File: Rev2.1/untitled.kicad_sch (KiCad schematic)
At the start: 29 parts, among them SW1 SW_Push, SW2 SW_SPDT, U5 AMS1117-3.3, Y1 16MHz

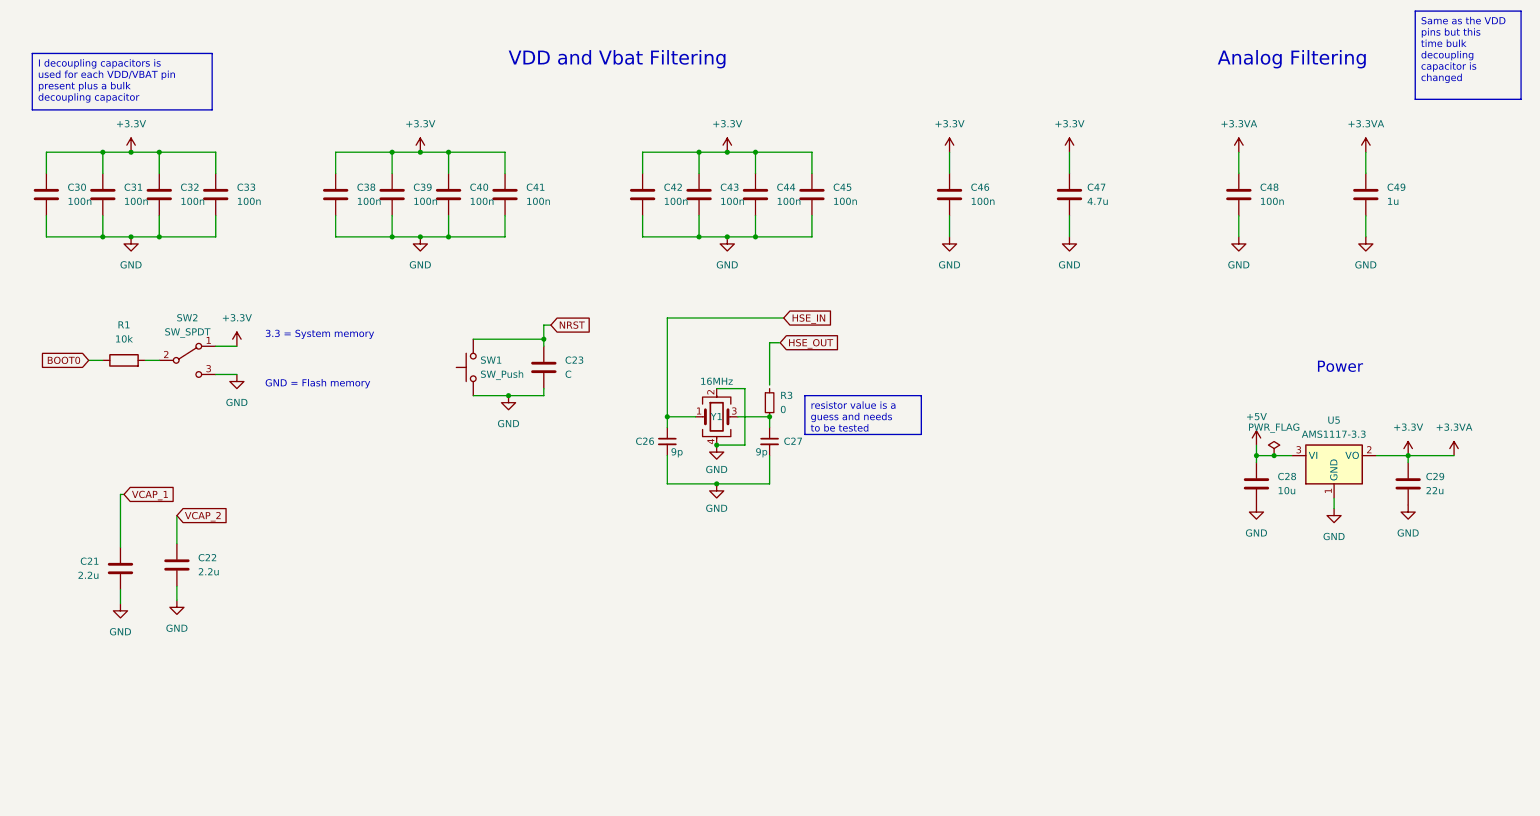
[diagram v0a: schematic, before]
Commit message: re-adding files something happened with last commit
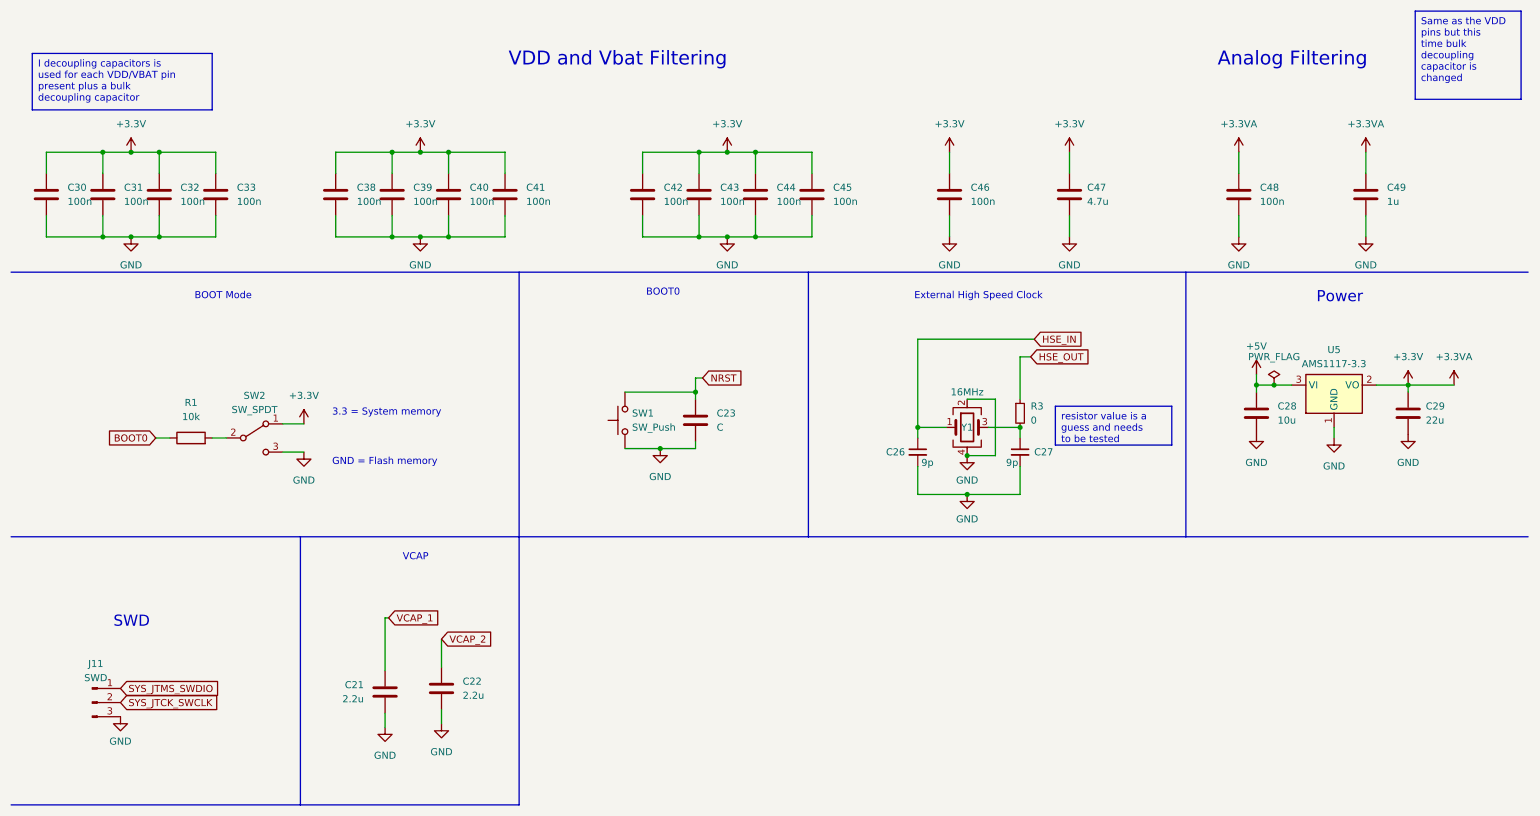
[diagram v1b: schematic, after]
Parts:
- added J11: SWD, Connector_PinHeader_2.54mm:PinHeader_1x03_P2.54mm_Vertical, symbol Connector:Conn_01x03_Pin
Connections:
- net GND: now also J11.3 (Pin_3)
- net HSE_OUT: now also R3.1
- new net SYS_JTCK_SWCLK: J11.2 (Pin_2)
- new net SYS_JTMS_SWDIO: J11.1 (Pin_1)
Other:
- note added: "BOOT Mode"
- note added: "BOOT0"
- note added: "External High Speed Clock"
- note added: "SWD"
- note added: "VCAP"
- moved on the sheet: C21, C22, C23, C26, C27, C28, C29, R1, R3, SW1, SW2, U5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

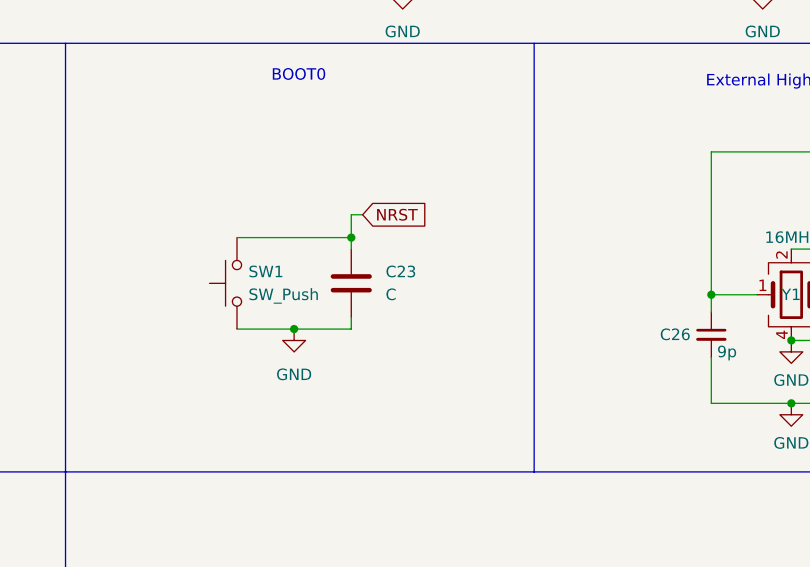
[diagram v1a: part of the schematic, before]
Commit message: finished the schematic and footprint assignment
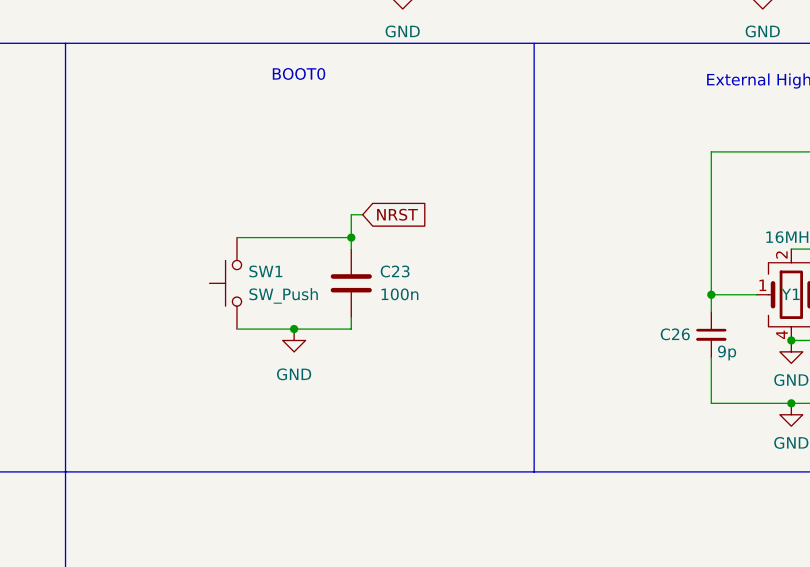
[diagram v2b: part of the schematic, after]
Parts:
- C23: value C -> 100n
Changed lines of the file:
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@@
   (symbol (lib_id "Device:C") (at 135.255 88.265 0) (unit 1)
     (in_bom yes) (on_board yes) (dnp no) (fields_autoplaced)
-    (property "Reference" "C23" (at 139.065 86.995 0)
+    (property "Reference" "C23" (at 138.43 86.995 0)
       (effects (font (size 1.27 1.27)) (justify left))
     )
-    (property "Value" "C" (at 139.065 89.535 0)
+    (property "Value" "100n" (at 138.43 89.535 0)
       (effects (font (size 1.27 1.27)) (justify left))
     )
